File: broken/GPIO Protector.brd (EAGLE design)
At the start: 53 x 62.2 mm, 19 parts

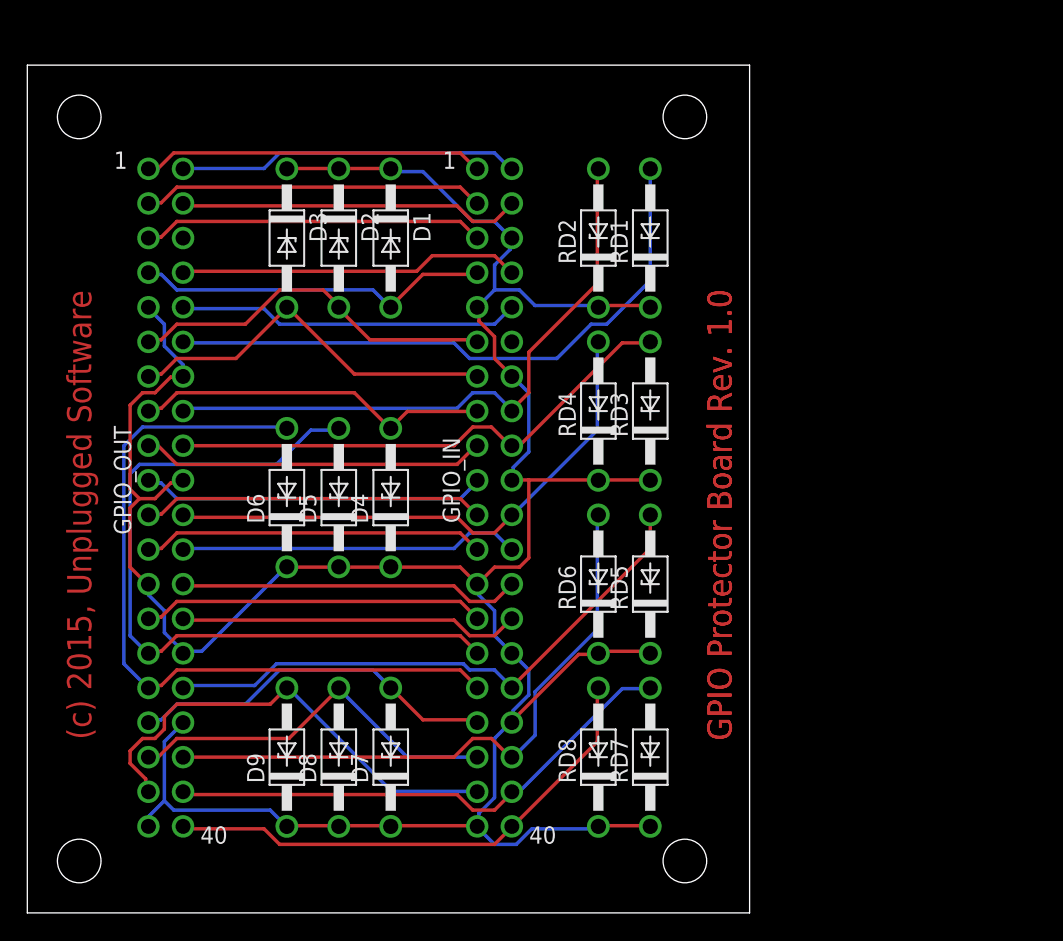
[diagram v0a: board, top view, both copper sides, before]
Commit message: Moved some things to broken for now. May fix them later.
Added console to split protector in GPIO Split Protector with Console.

Added Arduino Detectors shield.
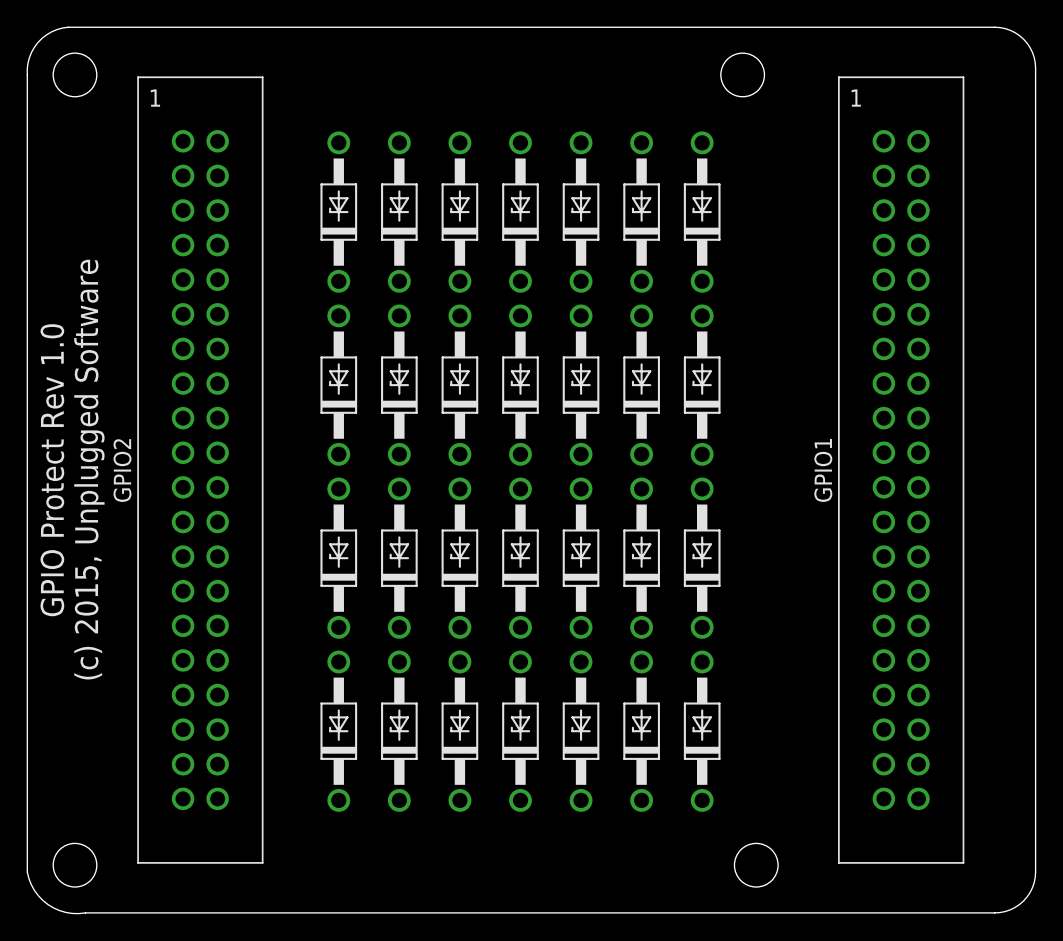
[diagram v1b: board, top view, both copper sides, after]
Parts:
- removed GPIO_IN, GPIO_OUT: RPI_GPIOUPPER, connectors:RPI_GPIO_MALE
- removed RD1, RD2, RD3, RD4, RD5, RD6, RD7, RD8: 3.3V, diode:DO41Z10
- added D10, D11, D12, D13, D14, D15, D16, D17, D18, D19, D20, D21, D22, D23, D24, D25, D26, D27, D28: 3.3V, diode:DO41Z10
- added GPIO1, GPIO2: RPI_GPIOUPPER, connectors:RPI_GPIO_MALE
- moved D8 32.6 mm to (40.6, 38.7)
- moved D6 30.8 mm to (49.5, 26.0)
- moved D5 30.5 mm to (45.1, 51.4)
- moved D9 30.5 mm to (49.5, 13.3)
- moved D2 28.8 mm to (49.5, 38.7), turned to 90 degrees
- moved D7 27.8 mm to (31.8, 38.7)
- moved D4 23.0 mm to (36.2, 51.4)
- moved D1 22.9 mm to (49.5, 51.4), turned to 90 degrees
- moved D3 8.47 mm to (27.3, 51.4), turned to 90 degrees
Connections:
- removed net 3.3VDC1: GPIO_IN.1_3.3VDC, GPIO_OUT.1_3.3VDC
- removed net 3.3VDC2: GPIO_IN.17_3.3VDC, GPIO_OUT.17_3.3VDC
- removed net 5VDC1: GPIO_IN.2_5VDC, GPIO_OUT.2_5VDC
- removed net 5VDC2: GPIO_IN.4_5VDC, GPIO_OUT.4_5VDC
- removed net 6_GND: GPIO_OUT.6_GND
- removed net I2C1_SCL: GPIO_IN.5_I2C1_SCL, GPIO_OUT.5_I2C1_SCL
- removed net I2C1_SDA: GPIO_IN.3_I2C1_SDA, GPIO_OUT.3_I2C1_SDA
- removed net SPI0_CE0: GPIO_IN.24_SPI0_CE0, GPIO_OUT.24_SPI0_CE0
- removed net SPI0_CE1: GPIO_IN.26_SPI0_CE1, GPIO_OUT.26_SPI0_CE1
- removed net SPI0_MOSI: GPIO_IN.19_SPI0_MOSI, GPIO_OUT.19_SPI0_MOSI
- removed net SPI0_SCLK: GPIO_IN.23_SPI0_SCLK, GPIO_OUT.23_SPI0_SCLK
- removed net SPIO_MISO: GPIO_IN.21_SPI0_MISO, GPIO_OUT.21_SPI0_MISO
- new net 3.3VDC: GPIO1.17_3.3VDC, GPIO1.1_3.3VDC, GPIO2.17_3.3VDC, GPIO2.1_3.3VDC
- new net 5VDC: GPIO1.2_5VDC, GPIO1.4_5VDC, GPIO2.2_5VDC, GPIO2.4_5VDC
- new net I2C_SCL: D2.A, GPIO1.5_I2C1_SCL, GPIO2.5_I2C1_SCL
- new net I2C_SDA: D1.A, GPIO1.3_I2C1_SDA, GPIO2.3_I2C1_SDA
- new net SPI_CE0: D22.A, GPIO1.24_SPI0_CE0, GPIO2.24_SPI0_CE0
- new net SPI_CE1: D23.A, GPIO1.26_SPI0_CE1, GPIO2.26_SPI0_CE1
- new net SPI_MISO: D8.A, GPIO1.21_SPI0_MISO, GPIO2.21_SPI0_MISO
- new net SPI_MOSI: D7.A, GPIO1.19_SPI0_MOSI, GPIO2.19_SPI0_MOSI
- new net SPI_SCLK: D9.A, GPIO1.23_SPI0_SCLK, GPIO2.23_SPI0_SCLK
- net GND: now also D10.C, D11.C, D12.C, D13.C, D14.C, D15.C, D16.C, D17.C, D18.C, D19.C, D20.C, D21.C, D22.C, D23.C, D24.C, D25.C, D26.C, D27.C, D28.C, GPIO1.14_GND, GPIO1.20_GND, GPIO1.25_GND, GPIO1.30_GND, GPIO1.34_GND, GPIO1.39_GND, GPIO1.6_GND, GPIO1.9_GND, GPIO2.14_GND, GPIO2.20_GND, GPIO2.25_GND, GPIO2.30_GND, GPIO2.34_GND, GPIO2.39_GND, GPIO2.6_GND, GPIO2.9_GND; no longer GPIO_IN.14_GND, GPIO_IN.20_GND, GPIO_IN.25_GND, GPIO_IN.30_GND, GPIO_IN.34_GND, GPIO_IN.39_GND, GPIO_IN.6_GND, GPIO_IN.9_GND, GPIO_OUT.14_GND, GPIO_OUT.20_GND, GPIO_OUT.25_GND, GPIO_OUT.30_GND, GPIO_OUT.34_GND, GPIO_OUT.39_GND, GPIO_OUT.9_GND, RD1.C, RD2.C, RD3.C, RD4.C, RD5.C, RD6.C, RD7.C, RD8.C
- net GPIO12: now also D25.A, GPIO1.32_GPIO12, GPIO2.32_GPIO12; no longer GPIO_IN.32_GPIO12, GPIO_OUT.32_GPIO12, RD5.A
- net GPIO13: now also D13.A, GPIO1.33_GPIO13, GPIO2.33_GPIO13; no longer D7.A, GPIO_IN.33_GPIO13, GPIO_OUT.33_GPIO13
- net GPIO16: now also D26.A, GPIO1.36_GPIO16, GPIO2.36_GPIO16; no longer GPIO_IN.36_GPIO16, GPIO_OUT.36_GPIO16, RD6.A
- net GPIO17: now also D4.A, GPIO1.11_GPIO17, GPIO2.11_GPIO17; no longer D2.A, GPIO_IN.11_GPIO17, GPIO_OUT.11_GPIO17
- net GPIO18: now also D16.A, GPIO1.12_GPIO18, GPIO2.12_GPIO18; no longer GPIO_OUT.12_GPIO18, RD1.A
- net GPIO19: now also D14.A, GPIO1.35_GPIO19, GPIO2.35_GPIO19; no longer D8.A, GPIO_IN.35_GPIO19, GPIO_OUT.35_GPIO19
- net GPIO20: now also D27.A, GPIO1.38_GPIO20, GPIO2.38_GPIO20; no longer GPIO_IN.38_GPIO20, GPIO_OUT.38_GPIO20, RD7.A
- net GPIO21: now also D28.A, GPIO1.40_GPIO21, GPIO2.40_GPIO21; no longer GPIO_IN.40_GPIO21, GPIO_OUT.40_GPIO21, RD8.A
- net GPIO22: now also D6.A, GPIO1.15_GPIO22, GPIO2.15_GPIO22; no longer D4.A, GPIO_IN.15_GPIO22, GPIO_OUT.15_GPIO22
- net GPIO23: now also D17.A, GPIO1.16_GPIO23, GPIO2.16_GPIO23; no longer GPIO_IN.16_GPIO23, GPIO_OUT.16_GPIO23, RD2.A
- net GPIO24: now also D18.A, GPIO1.18_GPIO24, GPIO2.18_GPIO24; no longer GPIO_IN.18_GPIO24, GPIO_OUT.18_GPIO24, RD3.A
- net GPIO25: now also D19.A, GPIO1.22_GPIO25, GPIO2.22_GPIO25; no longer GPIO_IN.22_GPIO25, GPIO_OUT.22_GPIO25, RD4.A
- net GPIO26: now also D15.A, GPIO1.37_GPIO26, GPIO2.37_GPIO26; no longer D9.A, GPIO_IN.37_GPIO26, GPIO_OUT.37_GPIO26
- net GPIO27: now also D5.A, GPIO1.13_GPIO27, GPIO2.13_GPIO27; no longer D3.A, GPIO_IN.13_GPIO27, GPIO_OUT.13_GPIO27
- net GPIO4: now also D3.A, GPIO1.7_GPIO4, GPIO2.7_GPIO4; no longer D1.A, GPIO_IN.7_GPIO4, GPIO_OUT.7_GPIO4
- net GPIO5: now also D11.A, GPIO1.29_GPIO5; no longer D5.A, GPIO_IN.29_GPIO5, GPIO_OUT.29_GPIO5
- net GPIO6: now also D12.A, GPIO1.31_GPIO6, GPIO2.31_GPIO6; no longer D6.A, GPIO_IN.31_GPIO6, GPIO_OUT.31_GPIO6
- net ID_SC: now also D24.A, GPIO1.28_ID_SC_EEPROM, GPIO2.28_ID_SC_EEPROM; no longer GPIO_IN.28_ID_SC_EEPROM, GPIO_OUT.28_ID_SC_EEPROM
- net ID_SD: now also D10.A, GPIO1.27_ID_SD_EEPROM, GPIO2.27_ID_SD_EEPROM; no longer GPIO_IN.27_ID_SD_EEPROM, GPIO_OUT.27_ID_SD_EEPROM
- net UART_RXD: now also D21.A, GPIO1.10_UART_RXD, GPIO2.10_UART_RXD; no longer GPIO_IN.10_UART_RXD, GPIO_OUT.10_UART_RXD
- net UART_TXD: now also D20.A, GPIO1.8_UART_TXD, GPIO2.8_UART_TXD; no longer GPIO_IN.8_UART_TXD, GPIO_OUT.8_UART_TXD
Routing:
- net GND: track 212.1 -> 0.00 mm
- net GPIO6: track 56.5 -> 0.00 mm
- net GPIO5: track 55.8 -> 0.00 mm
- net GPIO23: track 45.8 -> 0.00 mm
- net GPIO16: track 45.7 -> 0.00 mm
- net GPIO18: track 45.4 -> 0.00 mm
- net GPIO12: track 42.6 -> 0.00 mm
- net GPIO25: track 40.7 -> 0.00 mm
- net GPIO20: track 38.7 -> 0.00 mm
- net GPIO24: track 38.6 -> 0.00 mm
- net GPIO21: track 38.2 -> 0.00 mm
- net GPIO26: track 34.7 -> 0.00 mm
- net GPIO27: track 28.4 -> 0.00 mm
- net GPIO19: track 28.4 -> 0.00 mm
- net GPIO17: track 27.5 -> 0.00 mm
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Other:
- board size 53 x 62.2 mm -> 74 x 65.1 mm
- board text added: "GPIO Protect Rev 1.0 (c) 2015, Unplugged Software"
- board text removed: "(c) 2015, Unplugged Software"
- board text removed: "GPIO Protector Board Rev. 1.0"
